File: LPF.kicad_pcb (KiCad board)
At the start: 4 copper layers, 100 x 100 mm, 110 parts, among them J1 Conn_02x05_Counter_Clockwise, P1 SMA, P3 SMA, P4 SMA

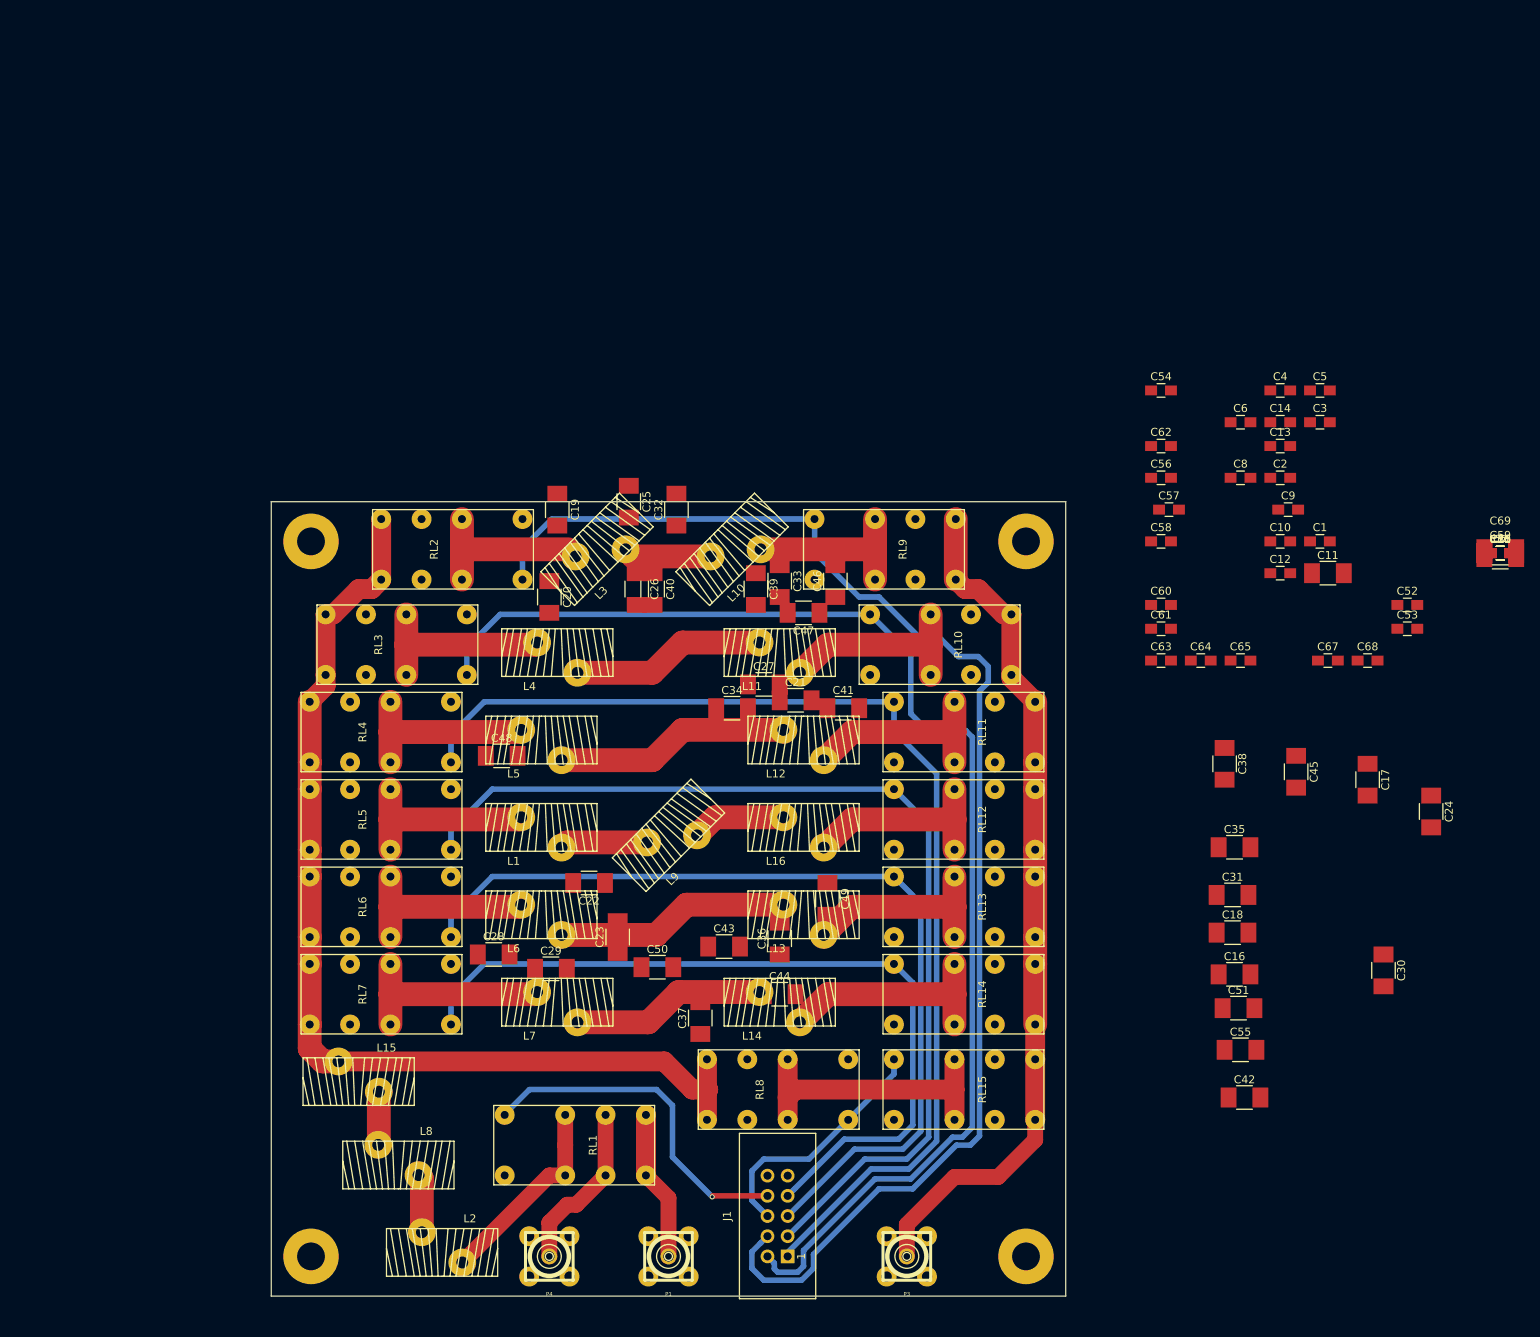
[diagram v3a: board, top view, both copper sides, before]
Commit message: decoupling & freewheeling routing
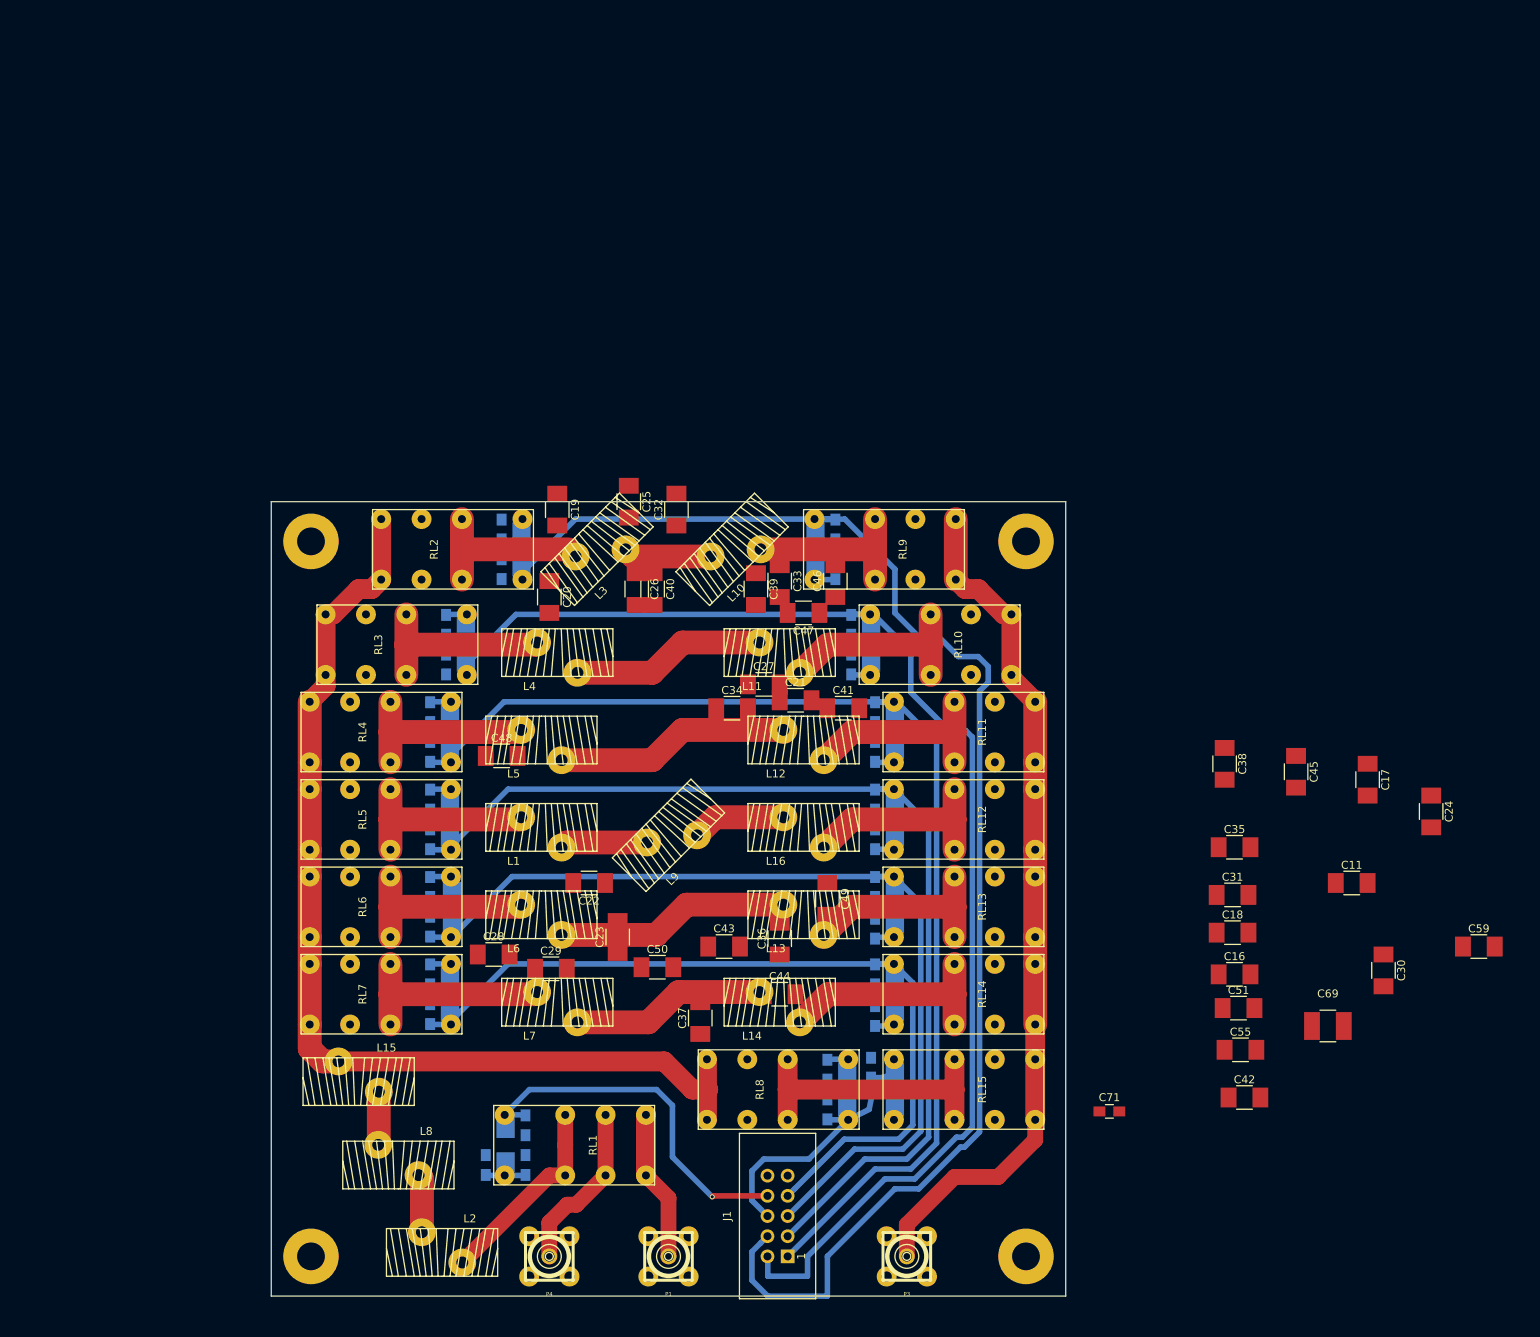
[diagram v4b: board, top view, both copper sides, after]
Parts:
- added D1: D, Diodes_SMD:D_SMB, B.Cu at (84.5, 126.0)
- added D10: D, Diodes_SMD:D_SMB, B.Cu at (130.5, 63.0)
- added D11: D, Diodes_SMD:D_SMB, B.Cu at (77.5, 85.0)
- added D12: D, Diodes_SMD:D_SMB, B.Cu at (77.8, 96.2)
- added D13: D, Diodes_SMD:D_SMB, B.Cu at (77.5, 107.0)
- added D14: D, Diodes_SMD:D_SMB, B.Cu at (133.5, 119.0)
- added D15: D, Diodes_SMD:D_SMB, B.Cu at (133.5, 74.0)
- added D2: D, Diodes_SMD:D_SMB, B.Cu at (86.5, 51.0)
- added D3: D, Diodes_SMD:D_SMB, B.Cu at (123.5, 51.0)
- added D4: D, Diodes_SMD:D_SMB, B.Cu at (79.5, 63.0)
- added D5: D, Diodes_SMD:D_SMB, B.Cu at (77.5, 74.0)
- added D6: D, Diodes_SMD:D_SMB, B.Cu at (133.5, 85.0)
- added D7: D, Diodes_SMD:D_SMB, B.Cu at (133.5, 96.0)
- added D8: D, Diodes_SMD:D_SMB, B.Cu at (133.5, 107.0)
- added D9: D, Diodes_SMD:D_SMB, B.Cu at (127.5, 119.0)
- C1, C10, C12, C13, C14, C15, C2, C3, C4, C5, C52, C53, C54, C56, C57, C58, C6, C60, C61, C62, C63, C64, C65, C66, C67, C68, C7, C70, C8, C9: moved to B.Cu
- moved C15 144.8 mm to (75.0, 104.5), turned to 270 degrees
- moved C7 142.3 mm to (87.0, 123.5), turned to 270 degrees
- moved C14 130.4 mm to (75.0, 109.5), turned to 90 degrees
- moved C5 128.3 mm to (75.0, 93.5), turned to 270 degrees
- moved C67 123.6 mm to (82.0, 128.5), turned to 90 degrees
- moved C68 123.6 mm to (87.0, 128.5), turned to 90 degrees
- moved C53 121.1 mm to (77.0, 65.5), turned to 270 degrees
- moved C4 118.7 mm to (75.0, 82.5), turned to 270 degrees
- moved C3 117.8 mm to (75.0, 71.5), turned to 270 degrees
- moved C10 110.2 mm to (75.0, 76.5), turned to 90 degrees
- moved C66 109.9 mm to (125.0, 121.5), turned to 90 degrees
- moved C57 106.8 mm to (75.0, 98.5), turned to 270 degrees
- moved C2 106.6 mm to (77.0, 60.5), turned to 270 degrees
- moved C1 103.0 mm to (84.0, 48.5), turned to 270 degrees
- moved C56 102.6 mm to (75.0, 87.5), turned to 270 degrees
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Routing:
- net +12V: track 4.43 -> 60.3 mm
- net 6m_Bypass: track 31.3 -> 41.7 mm
- net 160m: track 177.2 -> 186.6 mm
- net 40m: track 143.5 -> 150.8 mm
- net 30/20m: track 129.9 -> 137.2 mm
- net 17/15m: track 115.0 -> 121.8 mm
- net 12/10m: track 101.8 -> 108.5 mm
- net 80m: track 164.4 -> 169.4 mm
- net TX_RX_RLY: track 43.9 -> 48.2 mm

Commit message: RTM
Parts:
- removed C71: 10n, Capacitors_SMD:C_0805_HandSoldering
- C11, C16, C17, C18, C19, C20, C21, C22, C23, C24, C25, C26, C27, C28, C29, C30, C31, C32, C33, C34, C35, C36, C37, C38, C39, C40, C41, C42, C43, C44, C45, C46, C47, C48, C49, C50, C51, C55, C59, C69: moved to B.Cu
- moved C59 138.7 mm to (69.0, 114.5)
- moved C17 133.7 mm to (74.2, 141.5), turned to 180 degrees
- moved C24 132.1 mm to (78.5, 133.5), turned to 180 degrees
- moved C30 129.0 mm to (68.8, 130.2), turned to 180 degrees
- moved C45 127.0 mm to (63.8, 119.8), turned to 180 degrees
- moved C11 125.8 mm to (65.5, 85.0)
- moved C38 111.4 mm to (73.0, 122.8), turned to 180 degrees
- moved C16 90.8 mm to (86.8, 89.2)
- moved C18 83.7 mm to (93.5, 85.2), turned to 180 degrees
- moved C31 78.8 mm to (97.5, 88.0)
- moved C69 72.7 mm to (115.8, 119.0), turned to 180 degrees
- moved C42 72.2 mm to (114.5, 84.8)
- moved C35 72.1 mm to (104.2, 84.8)
- moved C51 60.3 mm to (119.8, 89.0)
- moved C55 58.0 mm to (126.5, 85.5), turned to 180 degrees
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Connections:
- C1 pad 1: +12V -> 160m
- C10 pad 1: 40m -> +12V
- C12 pad 1: 30/20m -> +12V
- C13 pad 1: 17/15m -> +12V
- C14 pad 1: 12/10m -> +12V
- C15 pad 1: +12V -> 6m_Bypass
- C2 pad 1: +12V -> 80m
- C3 pad 1: +12V -> 40m
- C4 pad 1: +12V -> 30/20m
- C5 pad 1: +12V -> 17/15m
- C6 pad 1: +12V -> 12/10m
- C66 pad 1: 6m_Bypass -> +12V
- C8 pad 1: 160m -> +12V
- C9 pad 1: 80m -> +12V
- D10 pad 1: 80m -> +12V
- D10 pad 2: +12V -> 80m
- D11 pad 1: 30/20m -> +12V
- D11 pad 2: +12V -> 30/20m
- D12 pad 1: 17/15m -> +12V
- D12 pad 2: +12V -> 17/15m
- D13 pad 1: 12/10m -> +12V
- D13 pad 2: +12V -> 12/10m
- D14 pad 1: 6m_Bypass -> +12V
- D14 pad 2: +12V -> 6m_Bypass
- D15 pad 1: 40m -> +12V
- D15 pad 2: +12V -> 40m
- D2 pad 1: 160m -> +12V
- D2 pad 2: +12V -> 160m
- RL2 pad 1: +12V -> 160m
- RL2 pad 16: 160m -> +12V
- RL3 pad 1: +12V -> 80m
- RL3 pad 16: 80m -> +12V
- RL4 pad 1: +12V -> 40m
- RL4 pad 16: 40m -> +12V
- RL5 pad 1: +12V -> 30/20m
- RL5 pad 16: 30/20m -> +12V
- RL6 pad 1: +12V -> 17/15m
- RL6 pad 16: 17/15m -> +12V
- RL7 pad 1: +12V -> 12/10m
- RL7 pad 16: 12/10m -> +12V
- RL8 pad 1: +12V -> 6m_Bypass
- RL8 pad 16: 6m_Bypass -> +12V
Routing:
- net GND: track 0.00 -> 996.0 mm, vias 0 -> 162
- net Net-(C17-Pad2): track 7.36 -> 25.9 mm
- net Net-(C23-Pad2): track 26.2 -> 41.6 mm
- net Net-(C22-Pad2): track 24.2 -> 39.6 mm
- net Net-(C21-Pad2): track 24.2 -> 39.6 mm
- net Net-(C20-Pad2): track 24.2 -> 39.5 mm
- net Net-(C11-Pad2): track 24.2 -> 39.5 mm
- net Net-(C19-Pad2): track 22.3 -> 35.9 mm
- net Net-(C16-Pad2): track 11.0 -> 23.4 mm
- net Net-(C35-Pad2): track 11.8 -> 23.0 mm
- net Net-(C29-Pad2): track 24.5 -> 35.6 mm
- net Net-(C26-Pad2): track 24.5 -> 35.6 mm
- net Net-(C28-Pad2): track 29.5 -> 40.3 mm
- net Net-(C27-Pad2): track 29.5 -> 40.3 mm
- net Net-(C30-Pad2): track 6.72 -> 17.3 mm
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- added copper zone on In1.Cu, net +12V
- added copper zone on B.Cu, net GND
- added copper zone on In2.Cu, net GND

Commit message: RTM 2, silk corrected, via added, jpg image and readme added
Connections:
- J1 pad 6: 6m_Bypass -> TX_RX_RLY
- J1 pad 8: TX_RX_RLY -> 6m_Bypass
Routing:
- net GND: track 996.0 -> 1204.5 mm, vias 162 -> 312
- net 6m_Bypass: track 41.9 -> 38.3 mm
- net TX_RX_RLY: track 48.2 -> 48.9 mm, vias 1 -> 0
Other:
- board text added: "12Vcc 10m 15m 20m 40m"
- board text added: "Alexiares LPF"
- board text added: "From P.A. Output"
- board text added: "Gnd 6m TX_Rly 160m 80m"
- board text added: "Gnd 6m-ByPass TX_Rly 160m 80m"
- board text added: "HF_TX"
- board text added: "LPF Out"
- board text added: "RX MASTER_IN"
- board text added: "Rx Master In"
- board text added: "Schematic KE9H/ VK6APH Drawing f6itu"
- board text added: "to PS/VSWR Ant. Brd TX Conn Brd"

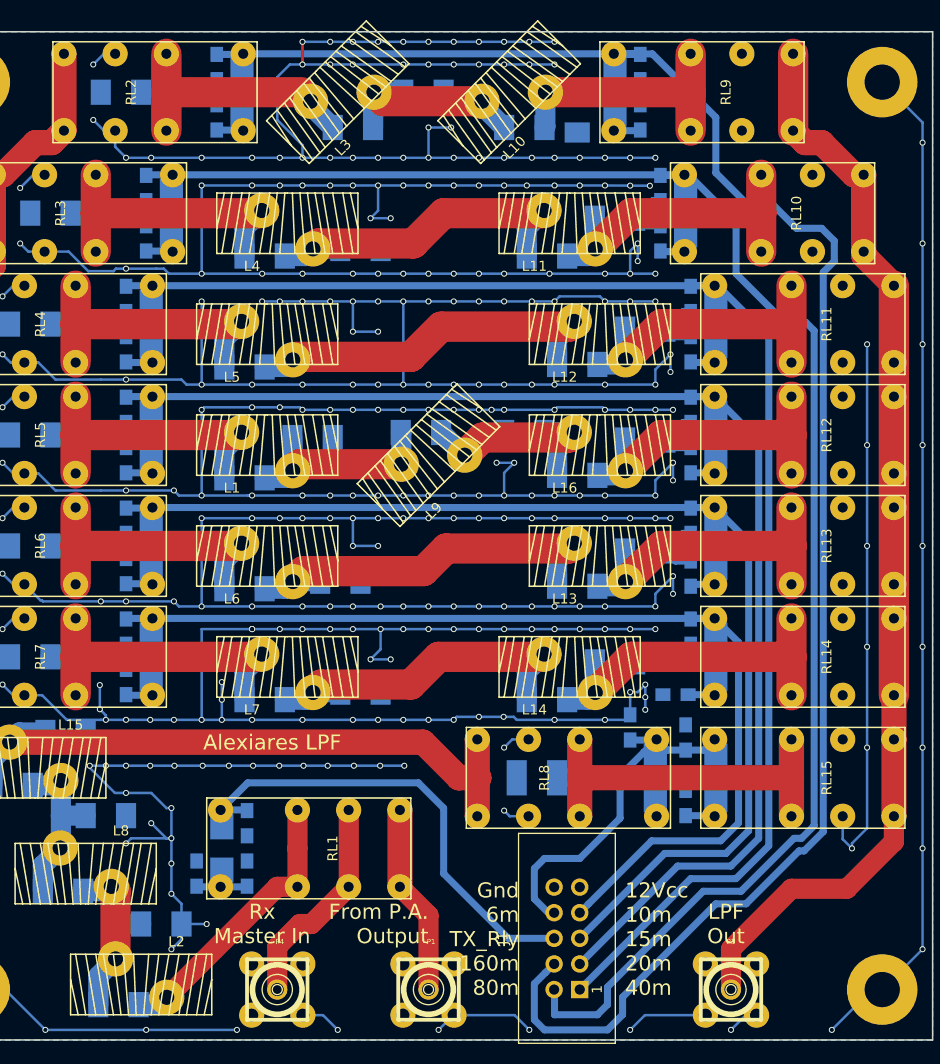
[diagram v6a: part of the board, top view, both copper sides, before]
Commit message: added choke ferrite on each command line
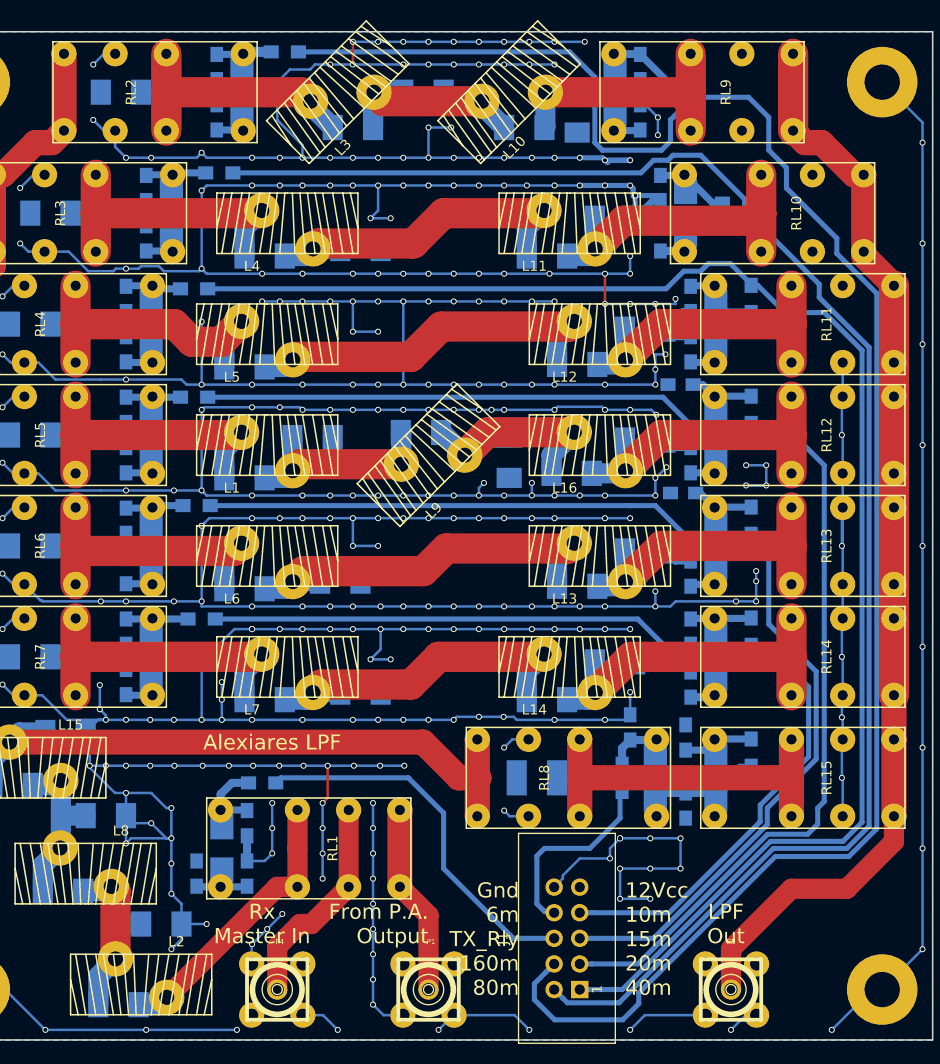
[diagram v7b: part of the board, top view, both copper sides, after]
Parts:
- added L17: Choke, Inductors_SMD:L_0805_HandSoldering, B.Cu at (88.5, 119.5)
- added L24: Choke, Inductors_SMD:L_0805_HandSoldering, B.Cu at (90.8, 47.0)
- added L25: Choke, Inductors_SMD:L_0805_HandSoldering, B.Cu at (84.2, 59.0)
- added L26: Choke, Inductors_SMD:L_0805_HandSoldering, B.Cu at (81.8, 70.5)
- added L27: Choke, Inductors_SMD:L_0805_HandSoldering, B.Cu at (81.8, 81.2)
- added L28: Choke, Inductors_SMD:L_0805_HandSoldering, B.Cu at (82.0, 92.0)
- added L29: Choke, Inductors_SMD:L_0805_HandSoldering, B.Cu at (82.5, 103.2)
- added L30: Choke, Inductors_SMD:L_0805_HandSoldering, B.Cu at (124.2, 119.0)
- added L31: Choke, Inductors_SMD:L_0805_HandSoldering, B.Cu at (129.8, 51.5)
- added L32: Choke, Inductors_SMD:L_0805_HandSoldering, B.Cu at (135.5, 62.0)
- added L33: Choke, Inductors_SMD:L_0805_HandSoldering, B.Cu at (137.0, 71.5)
- added L34: Choke, Inductors_SMD:L_0805_HandSoldering, B.Cu at (137.0, 82.5)
- added L35: Choke, Inductors_SMD:L_0805_HandSoldering, B.Cu at (137.0, 93.5)
- added L36: Choke, Inductors_SMD:L_0805_HandSoldering, B.Cu at (137.0, 104.5)
- added L37: Choke, Inductors_SMD:L_0805_HandSoldering, B.Cu at (137.0, 116.5)
- C69: value C -> 18p
- moved D11 56.0 mm to (133.5, 85.0)
- moved D12 56.0 mm to (133.5, 96.0)
- moved D13 56.0 mm to (133.5, 107.0)
- moved D6 56.0 mm to (77.5, 85.0)
- moved D7 56.0 mm to (77.5, 96.0)
- moved D8 56.0 mm to (77.5, 107.0)
- moved C42 2.92 mm to (113.0, 87.2), turned to 90 degrees
- moved C57 2.85 mm to (130.2, 90.8), turned to 0 degrees
- moved C56 2.69 mm to (130.0, 80.0), turned to 0 degrees
- moved C65 1.80 mm to (131.0, 109.8), turned to 90 degrees
- moved C51 0.59 mm to (119.2, 88.8)
- moved C66 0.25 mm to (130.5, 121.8), turned to 270 degrees
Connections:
- C1 pad 1: 160m -> Net-(C1-Pad1)
- C15 pad 1: 6m_Bypass -> Net-(C15-Pad1)
- C2 pad 1: 80m -> Net-(C2-Pad1)
- C3 pad 1: 40m -> Net-(C3-Pad1)
- C4 pad 1: 30/20m -> Net-(C4-Pad1)
- C5 pad 1: 17/15m -> Net-(C5-Pad1)
- C52 pad 2: 160m -> Net-(C52-Pad2)
- C53 pad 2: 80m -> Net-(C53-Pad2)
- C54 pad 2: 40m -> Net-(C54-Pad2)
- C56 pad 2: 30/20m -> Net-(C56-Pad2)
- C57 pad 2: 17/15m -> Net-(C57-Pad2)
- C58 pad 2: 12/10m -> Net-(C58-Pad2)
- C6 pad 1: 12/10m -> Net-(C6-Pad1)
- C7 pad 1: TX_RX_RLY -> Net-(C7-Pad1)
- C70 pad 2: 6m_Bypass -> Net-(C70-Pad2)
- D1 pad 2: TX_RX_RLY -> Net-(C7-Pad1)
- D10 pad 2: 80m -> Net-(C53-Pad2)
- D11 pad 2: 30/20m -> Net-(C56-Pad2)
- D12 pad 2: 17/15m -> Net-(C57-Pad2)
- D13 pad 2: 12/10m -> Net-(C58-Pad2)
- D14 pad 2: 6m_Bypass -> Net-(C70-Pad2)
- D15 pad 2: 40m -> Net-(C54-Pad2)
- D2 pad 2: 160m -> Net-(C52-Pad2)
- D3 pad 2: 160m -> Net-(C1-Pad1)
- D4 pad 2: 80m -> Net-(C2-Pad1)
- D5 pad 2: 40m -> Net-(C3-Pad1)
- D6 pad 2: 30/20m -> Net-(C4-Pad1)
- D7 pad 2: 17/15m -> Net-(C5-Pad1)
- D8 pad 2: 12/10m -> Net-(C6-Pad1)
- D9 pad 2: 6m_Bypass -> Net-(C15-Pad1)
- RL1 pad 16: TX_RX_RLY -> Net-(C7-Pad1)
- RL10 pad 16: 80m -> Net-(C53-Pad2)
- RL11 pad 16: 40m -> Net-(C54-Pad2)
- RL12 pad 16: 30/20m -> Net-(C56-Pad2)
- RL13 pad 16: 17/15m -> Net-(C57-Pad2)
- RL14 pad 16: 12/10m -> Net-(C58-Pad2)
- RL15 pad 16: 6m_Bypass -> Net-(C70-Pad2)
- RL2 pad 1: 160m -> Net-(C1-Pad1)
- RL3 pad 1: 80m -> Net-(C2-Pad1)
- RL4 pad 1: 40m -> Net-(C3-Pad1)
- RL5 pad 1: 30/20m -> Net-(C4-Pad1)
- RL6 pad 1: 17/15m -> Net-(C5-Pad1)
- RL7 pad 1: 12/10m -> Net-(C6-Pad1)
- RL8 pad 1: 6m_Bypass -> Net-(C15-Pad1)
- RL9 pad 16: 160m -> Net-(C52-Pad2)
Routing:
- net GND: track 1204.5 -> 1293.6 mm, vias 312 -> 338
- net Net-(C52-Pad2): track 0.00 -> 12.3 mm
- net TX_RX_RLY: track 48.9 -> 37.6 mm
- net Net-(C53-Pad2): track 0.00 -> 9.47 mm
- net Net-(C7-Pad1): track 0.00 -> 9.23 mm
- net Net-(C70-Pad2): track 0.00 -> 8.75 mm
- net 80m: track 167.8 -> 159.7 mm
- net Net-(C54-Pad2): track 0.00 -> 8.03 mm
- net Net-(C56-Pad2): track 0.00 -> 7.97 mm
- net Net-(C6-Pad1): track 0.00 -> 7.91 mm
- net Net-(C2-Pad1): track 0.00 -> 7.88 mm
- net Net-(C57-Pad2): track 0.00 -> 7.82 mm
- net Net-(C58-Pad2): track 0.00 -> 7.75 mm
- net Net-(C5-Pad1): track 0.00 -> 7.46 mm
- net Net-(C1-Pad1): track 0.00 -> 7.44 mm
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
